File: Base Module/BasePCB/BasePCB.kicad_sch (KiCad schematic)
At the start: 142 parts, among them J1 USB_A, J2 Conn_01x05_Female, J3 Conn_01x05_Male, SW1 SW_Push, U1 ATmega32U4-A, Y1 Crystal_GND24_Small

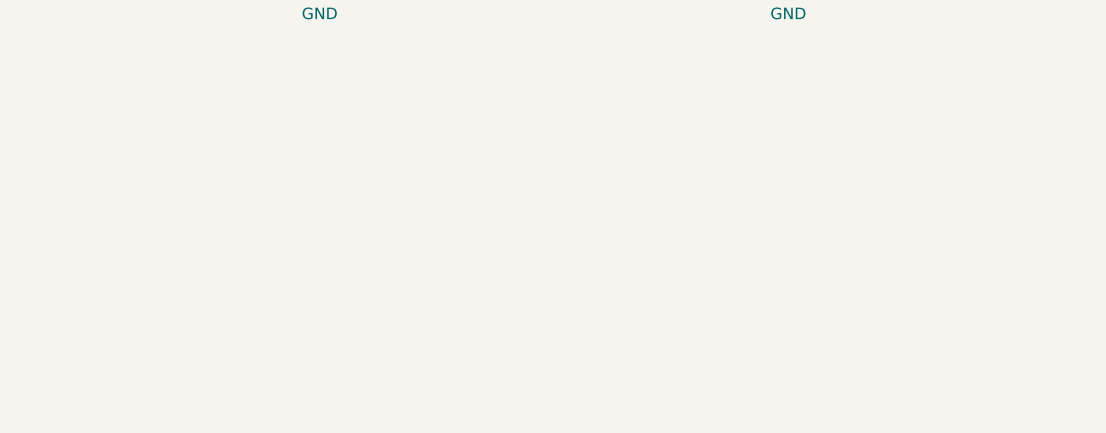
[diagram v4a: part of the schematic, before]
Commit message: Added additional connector
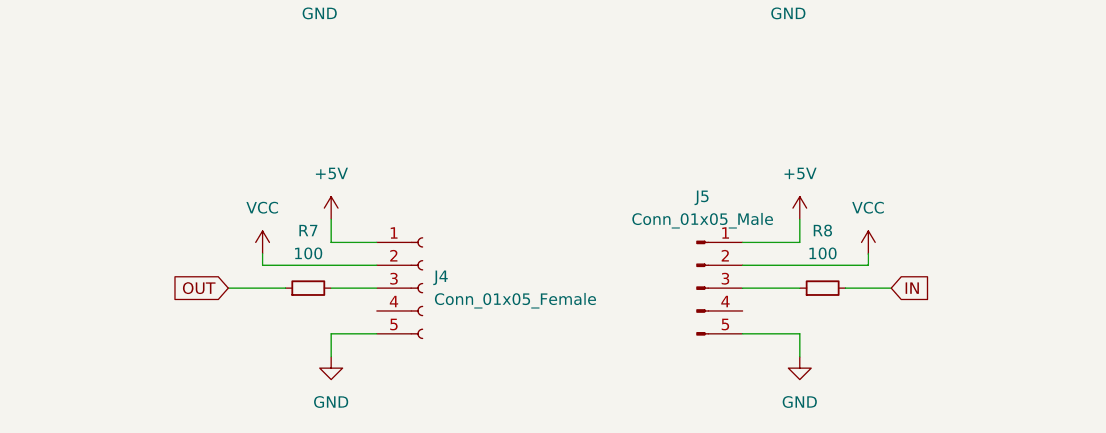
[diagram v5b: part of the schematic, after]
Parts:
- added J4: Conn_01x05_Female, Connector_JST:JST_PH_S5B-PH-K_1x05_P2.00mm_Horizontal, symbol Connector:Conn_01x05_Female
- added J5: Conn_01x05_Male, Connector_JST:JST_PH_S5B-PH-K_1x05_P2.00mm_Horizontal, symbol Connector:Conn_01x05_Male
- added R7, R8: 100, Resistor_SMD:R_0805_2012Metric, symbol Device:R_Small
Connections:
- net +5V: now also J4.1 (Pin_1), J5.1 (Pin_1)
- net GND: now also J4.5 (Pin_5), J5.5 (Pin_5)
- net IN: now also R8.2
- net OUT: now also R7.1
- net VCC: now also J4.2 (Pin_2), J5.2 (Pin_2)
- new net: J5.3 (Pin_3), R8.1
- new net: J4.3 (Pin_3), R7.2

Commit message: Made a few small changes
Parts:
- removed J5: Conn_01x05_Male, Connector_JST:JST_PH_S5B-PH-K_1x05_P2.00mm_Horizontal, symbol Connector:Conn_01x05_Male
- added J5: Conn_01x05_Female, Connector_JST:JST_PH_S5B-PH-K_1x05_P2.00mm_Horizontal, symbol Connector:Conn_01x05_Female
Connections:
- net +5V: now also J5.1 (Pin_1)
- net GND: now also J5.5 (Pin_5)
- net IN: no longer R8.2
- net OUT: now also R8.1
- net VCC: now also J5.2 (Pin_2)
- new net: J5.3 (Pin_3), R8.2
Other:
- note added: "USB-A"
- note removed: "USB-C"

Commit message: Edited connectors
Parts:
- removed J2, J4, J5: Conn_01x05_Female, Connector_JST:JST_PH_S5B-PH-K_1x05_P2.00mm_Horizontal, symbol Connector:Conn_01x05_Female
- removed J3: Conn_01x05_Male, Connector_JST:JST_PH_S5B-PH-K_1x05_P2.00mm_Horizontal, symbol Connector:Conn_01x05_Male
- removed R5, R6, R7, R8: 100, Resistor_SMD:R_0805_2012Metric, symbol Device:R_Small
- added J2: Conn_01x19_Female, Connector_JST:JST_SH_SM20B-SRSS-TB_1x20-1MP_P1.00mm_Horizontal, symbol Connector:Conn_01x19_Female
- added J3: Conn_01x19_Male, Connector_JST:JST_SH_SM20B-SRSS-TB_1x20-1MP_P1.00mm_Horizontal, symbol Connector:Conn_01x19_Male
- added J4: Conn_01x18_Female, Connector_JST:JST_SH_SM20B-SRSS-TB_1x20-1MP_P1.00mm_Horizontal, symbol Connector:Conn_01x18_Female
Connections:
- net +5V: now also J2.1 (Pin_1), J3.1 (Pin_1), J4.1 (Pin_1)
- net COL0: now also J2.3 (Pin_3), J3.3 (Pin_3), J4.3 (Pin_3)
- net COL1: now also J2.4 (Pin_4), J3.4 (Pin_4), J4.4 (Pin_4)
- net COL10: now also J2.13 (Pin_13), J3.13 (Pin_13), J4.13 (Pin_13)
- net COL11: now also J4.14 (Pin_14)
- net COL12: now also J4.15 (Pin_15)
- net COL13: now also J4.16 (Pin_16)
- net COL2: now also J2.5 (Pin_5), J3.5 (Pin_5), J4.5 (Pin_5)
- net COL3: now also J2.6 (Pin_6), J3.6 (Pin_6), J4.6 (Pin_6)
- net COL4: now also J2.7 (Pin_7), J3.7 (Pin_7), J4.7 (Pin_7)
- net COL5: now also J2.8 (Pin_8), J3.8 (Pin_8), J4.8 (Pin_8)
- net COL6: now also J2.9 (Pin_9), J3.9 (Pin_9), J4.9 (Pin_9)
- net COL7: now also J2.10 (Pin_10), J3.10 (Pin_10), J4.10 (Pin_10)
- net COL8: now also J2.11 (Pin_11), J3.11 (Pin_11), J4.11 (Pin_11)
- net COL9: now also J2.12 (Pin_12), J3.12 (Pin_12), J4.12 (Pin_12)
- net GND: now also J2.19 (Pin_19), J3.19 (Pin_19), J4.18 (Pin_18)
- net VCC: now also J2.2 (Pin_2), J3.2 (Pin_2), J4.2 (Pin_2)
- net ROW10: now reaches U1.1 (PE6)
- net ROW10: now also J4.17 (Pin_17)
- net ROW7: now reaches U1.36 (PF7)
- net ROW7: now also J2.16 (Pin_16), J3.16 (Pin_16)
- net ROW6: now reaches U1.37 (PF6)
- net ROW6: now also J2.15 (Pin_15), J3.15 (Pin_15)
- net ROW5: now reaches U1.38 (PF5)
- net ROW5: now also J2.14 (Pin_14), J3.14 (Pin_14)
- net IN renamed ROW8
- net ROW8: now also J2.17 (Pin_17), J3.17 (Pin_17)
- net OUT renamed ROW9
- net ROW9: now also J2.18 (Pin_18), J3.18 (Pin_18)
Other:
- moved on the sheet: F1, J1

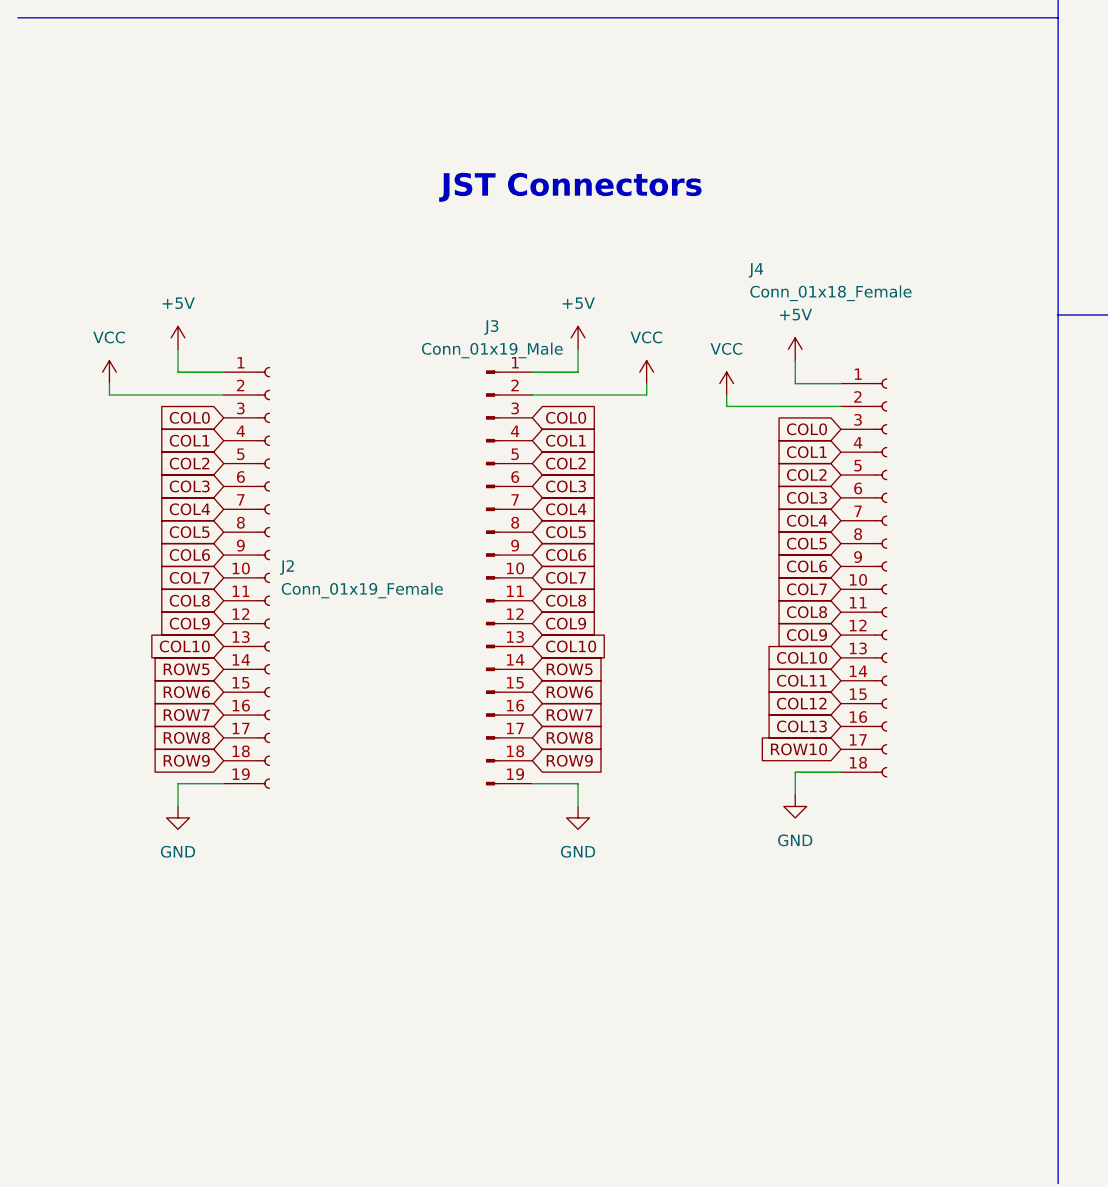
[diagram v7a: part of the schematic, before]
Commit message: Updated conenctors
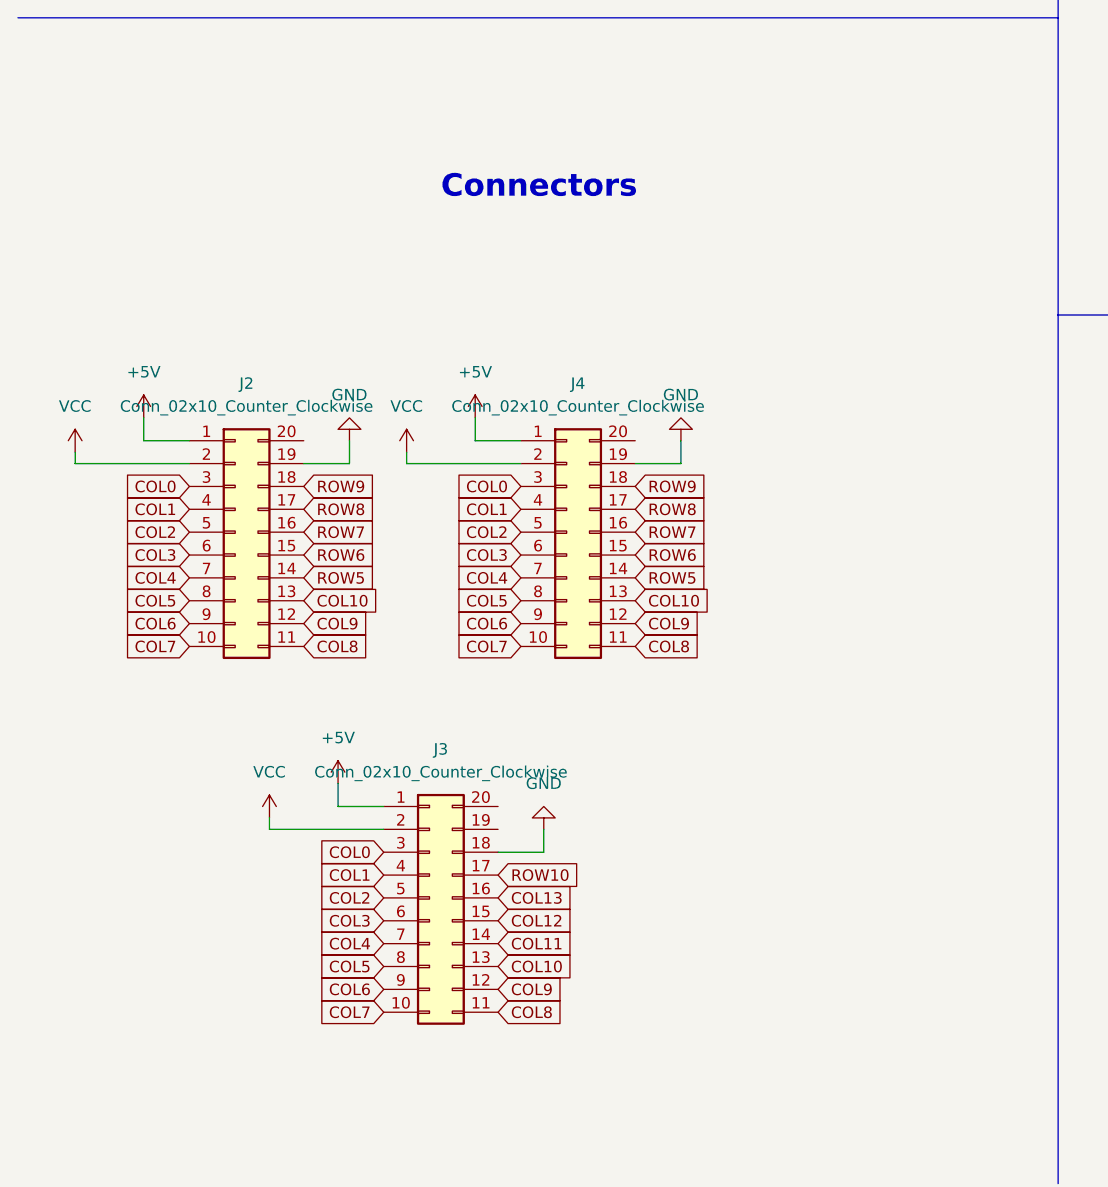
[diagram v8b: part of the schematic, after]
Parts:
- removed J2: Conn_01x19_Female, Connector_JST:JST_SH_SM20B-SRSS-TB_1x20-1MP_P1.00mm_Horizontal, symbol Connector:Conn_01x19_Female
- removed J3: Conn_01x19_Male, Connector_JST:JST_SH_SM20B-SRSS-TB_1x20-1MP_P1.00mm_Horizontal, symbol Connector:Conn_01x19_Male
- removed J4: Conn_01x18_Female, Connector_JST:JST_SH_SM20B-SRSS-TB_1x20-1MP_P1.00mm_Horizontal, symbol Connector:Conn_01x18_Female
- added J2, J3: Conn_02x10_Counter_Clockwise, Connector_PinSocket_2.54mm:PinSocket_2x10_P2.54mm_Horizontal, symbol Connector_Generic:Conn_02x10_Counter_Clockwise
- added J4: Conn_02x10_Counter_Clockwise, Connector_PinHeader_2.54mm:PinHeader_2x10_P2.54mm_Horizontal, symbol Connector_Generic:Conn_02x10_Counter_Clockwise
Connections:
- net +5V: now also J2.1 (Pin_1), J3.1 (Pin_1), J4.1 (Pin_1)
- net COL0: now also J2.3 (Pin_3), J3.3 (Pin_3), J4.3 (Pin_3)
- net COL1: now also J2.4 (Pin_4), J3.4 (Pin_4), J4.4 (Pin_4)
- net COL10: now also J2.13 (Pin_13), J3.13 (Pin_13), J4.13 (Pin_13)
- net COL11: now also J3.14 (Pin_14)
- net COL12: now also J3.15 (Pin_15)
- net COL13: now also J3.16 (Pin_16)
- net COL2: now also J2.5 (Pin_5), J3.5 (Pin_5), J4.5 (Pin_5)
- net COL3: now also J2.6 (Pin_6), J3.6 (Pin_6), J4.6 (Pin_6)
- net COL4: now also J2.7 (Pin_7), J3.7 (Pin_7), J4.7 (Pin_7)
- net COL5: now also J2.8 (Pin_8), J3.8 (Pin_8), J4.8 (Pin_8)
- net COL6: now also J2.9 (Pin_9), J3.9 (Pin_9), J4.9 (Pin_9)
- net COL7: now also J2.10 (Pin_10), J3.10 (Pin_10), J4.10 (Pin_10)
- net COL8: now also J2.11 (Pin_11), J3.11 (Pin_11), J4.11 (Pin_11)
- net COL9: now also J2.12 (Pin_12), J3.12 (Pin_12), J4.12 (Pin_12)
- net GND: now also J2.19 (Pin_19), J3.18 (Pin_18), J4.19 (Pin_19)
- net ROW10: now also J3.17 (Pin_17)
- net ROW5: now also J2.14 (Pin_14), J4.14 (Pin_14)
- net ROW6: now also J2.15 (Pin_15), J4.15 (Pin_15)
- net ROW7: now also J2.16 (Pin_16), J4.16 (Pin_16)
- net ROW8: now also J2.17 (Pin_17), J4.17 (Pin_17)
- net ROW9: now also J2.18 (Pin_18), J4.18 (Pin_18)
- net VCC: now also J2.2 (Pin_2), J3.2 (Pin_2), J4.2 (Pin_2)
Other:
- note added: "Connectors"
- note removed: "JST Connectors"
